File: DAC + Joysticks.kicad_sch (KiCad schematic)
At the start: 127 parts, among them J10 L Phono, J11 R Phono, J8 JOY0, J9 JOY1, U23 74HC374, U24 74HC374, U25 74HC244, U26 74HC244, U27 74HC373, U28 74HC244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

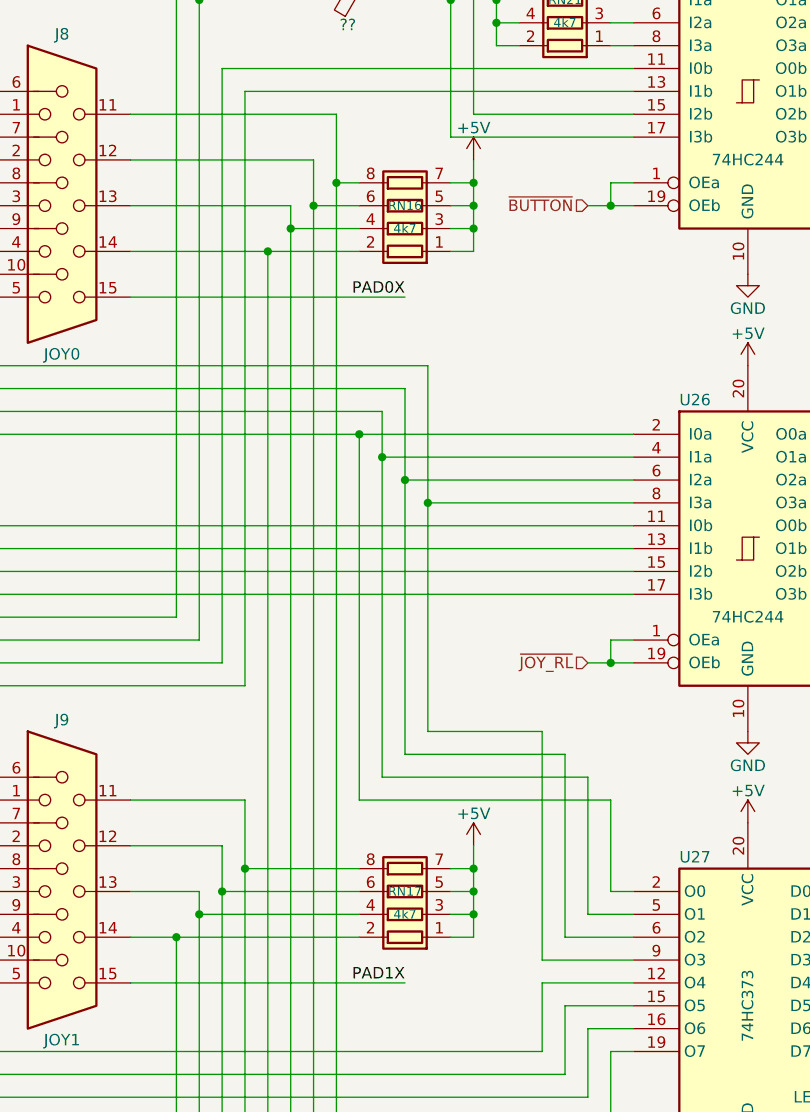
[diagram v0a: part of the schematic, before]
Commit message: motherboard: Routing for the joystick ports
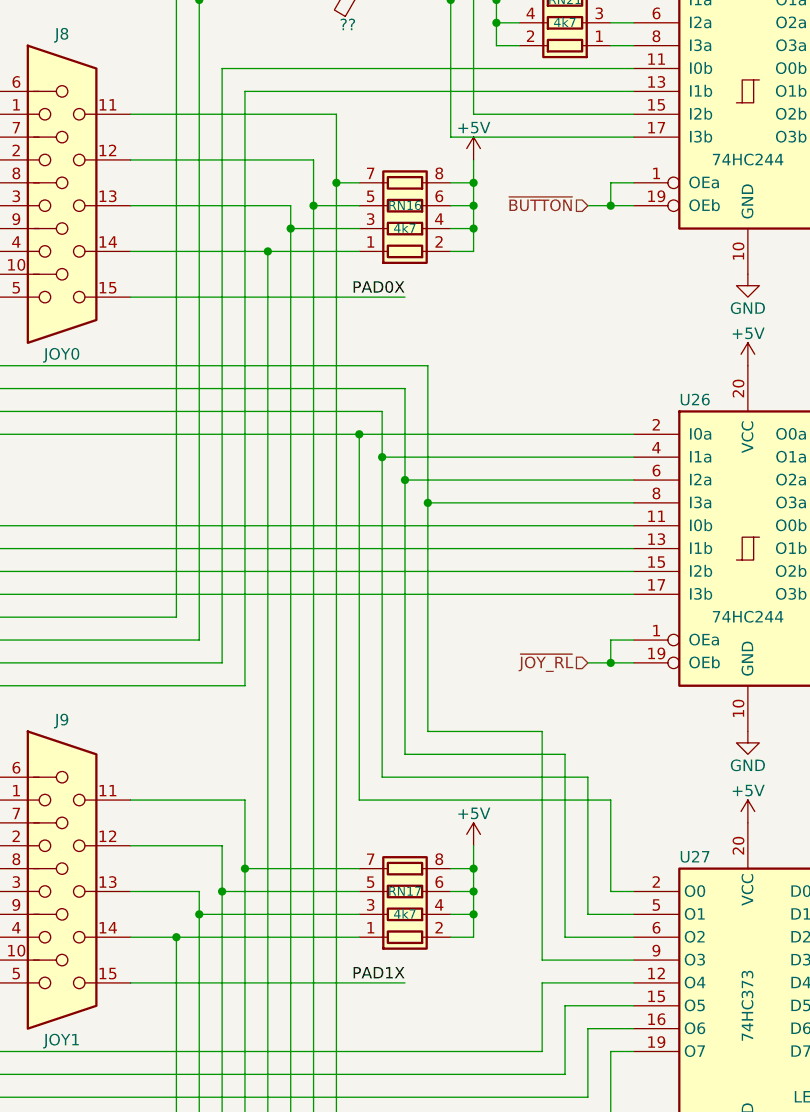
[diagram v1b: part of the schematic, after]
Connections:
- net +5V: now also RN16.2 (R2.1), RN16.4 (R4.1), RN16.6 (R3.2), RN16.8 (R1.2), RN17.2 (R2.1), RN17.4 (R4.1), RN17.6 (R3.2), RN17.8 (R1.2); no longer RN16.1 (R1.1), RN16.3 (R3.1), RN16.5 (R4.2), RN16.7 (R2.2), RN17.1 (R1.1), RN17.3 (R3.1), RN17.5 (R4.2), RN17.7 (R2.2)
- net at J9.14, U28.11 (I0b): now also RN17.1 (R1.1); no longer RN17.2 (R2.1)
- net at J9.13, U28.13 (I1b): now also RN17.3 (R3.1); no longer RN17.4 (R4.1)
- net at J9.12, U28.15 (I2b): now also RN17.5 (R4.2); no longer RN17.6 (R3.2)
- net at J9.11, U28.17 (I3b): now also RN17.7 (R2.2); no longer RN17.8 (R1.2)
- net at J8.14, U28.2 (I0a): now also RN16.1 (R1.1); no longer RN16.2 (R2.1)
- net at J8.13, U28.4 (I1a): now also RN16.3 (R3.1); no longer RN16.4 (R4.1)
- net at J8.12, U28.6 (I2a): now also RN16.5 (R4.2); no longer RN16.6 (R3.2)
- net at J8.11, U28.8 (I3a): now also RN16.7 (R2.2); no longer RN16.8 (R1.2)
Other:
- moved on the sheet: RN16, RN17
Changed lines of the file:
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@@
 	(symbol
 		(lib_id "dragonmux:R_Pack04_OddEven")
-		(at 101.6 63.5 90)
+		(at 101.6 63.5 270)
+		(mirror x)
 		(unit 1)
 		(exclude_from_sim no)
@@
 		)
 		(property "Description" "4 resistor network, parallel topology"
-			(at 114.3 64.77 0)
+			(at 88.9 64.77 0)
 			(effects
 				(font
@@
 	(symbol
 		(lib_id "dragonmux:R_Pack04_OddEven")
-		(at 101.6 139.7 90)
+		(at 101.6 139.7 270)
+		(mirror x)
 		(unit 1)
 		(exclude_from_sim no)
@@
 		)
 		(property "Description" "4 resistor network, parallel topology"
-			(at 114.3 140.97 0)
+			(at 88.9 140.97 0)
 			(effects
 				(font

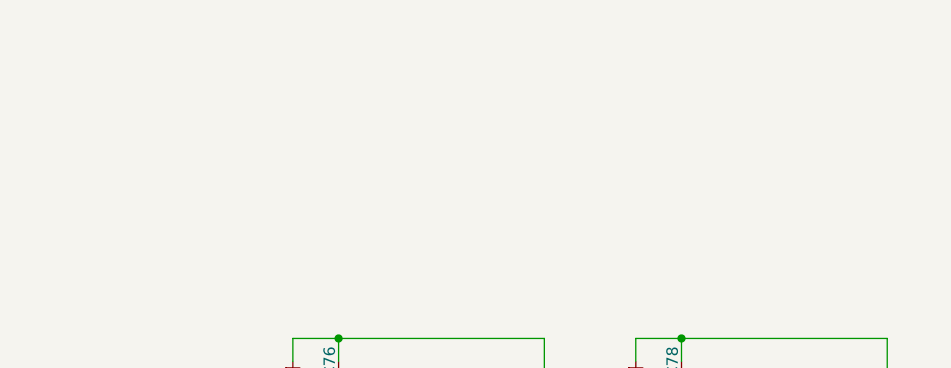
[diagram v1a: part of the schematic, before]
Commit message: motherboard: Added a note about how the FCLK signal works and how the Butterworth filter cutoffs work
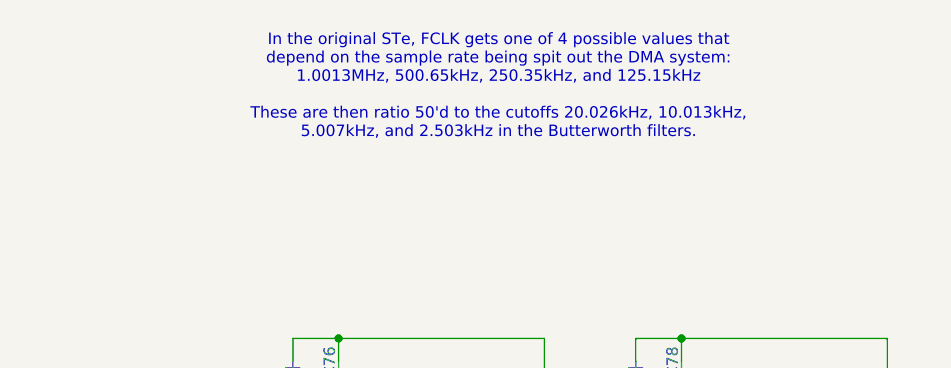
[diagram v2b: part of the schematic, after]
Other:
- note added: "In the original STe, FCLK gets one of 4 possible values that depend on the sample rate being spit out the DMA system: 1.0013MHz, 500.65kHz, 250.35kHz, and 125.15kHz These are then ratio 50'd to the cutoffs 20.026kHz, 10.013kHz, 5.007kHz, and 2.503kHz in the Butterworth filters."
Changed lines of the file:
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@@
 		(members "D[0..7]")
+	)
+	(text "In the original STe, FCLK gets one of 4 possible values that\ndepend on the sample rate being spit out the DMA system:\n1.0013MHz, 500.65kHz, 250.35kHz, and 125.15kHz\n\nThese are then ratio 50'd to the cutoffs 20.026kHz, 10.013kHz,\n5.007kHz, and 2.503kHz in the Butterworth filters."
+		(exclude_from_sim no)
+		(at 355.6 25.4 0)
+		(effects
+			(font
+				(size 1.27 1.27)
+			)
+		)
 	)
 	(junction

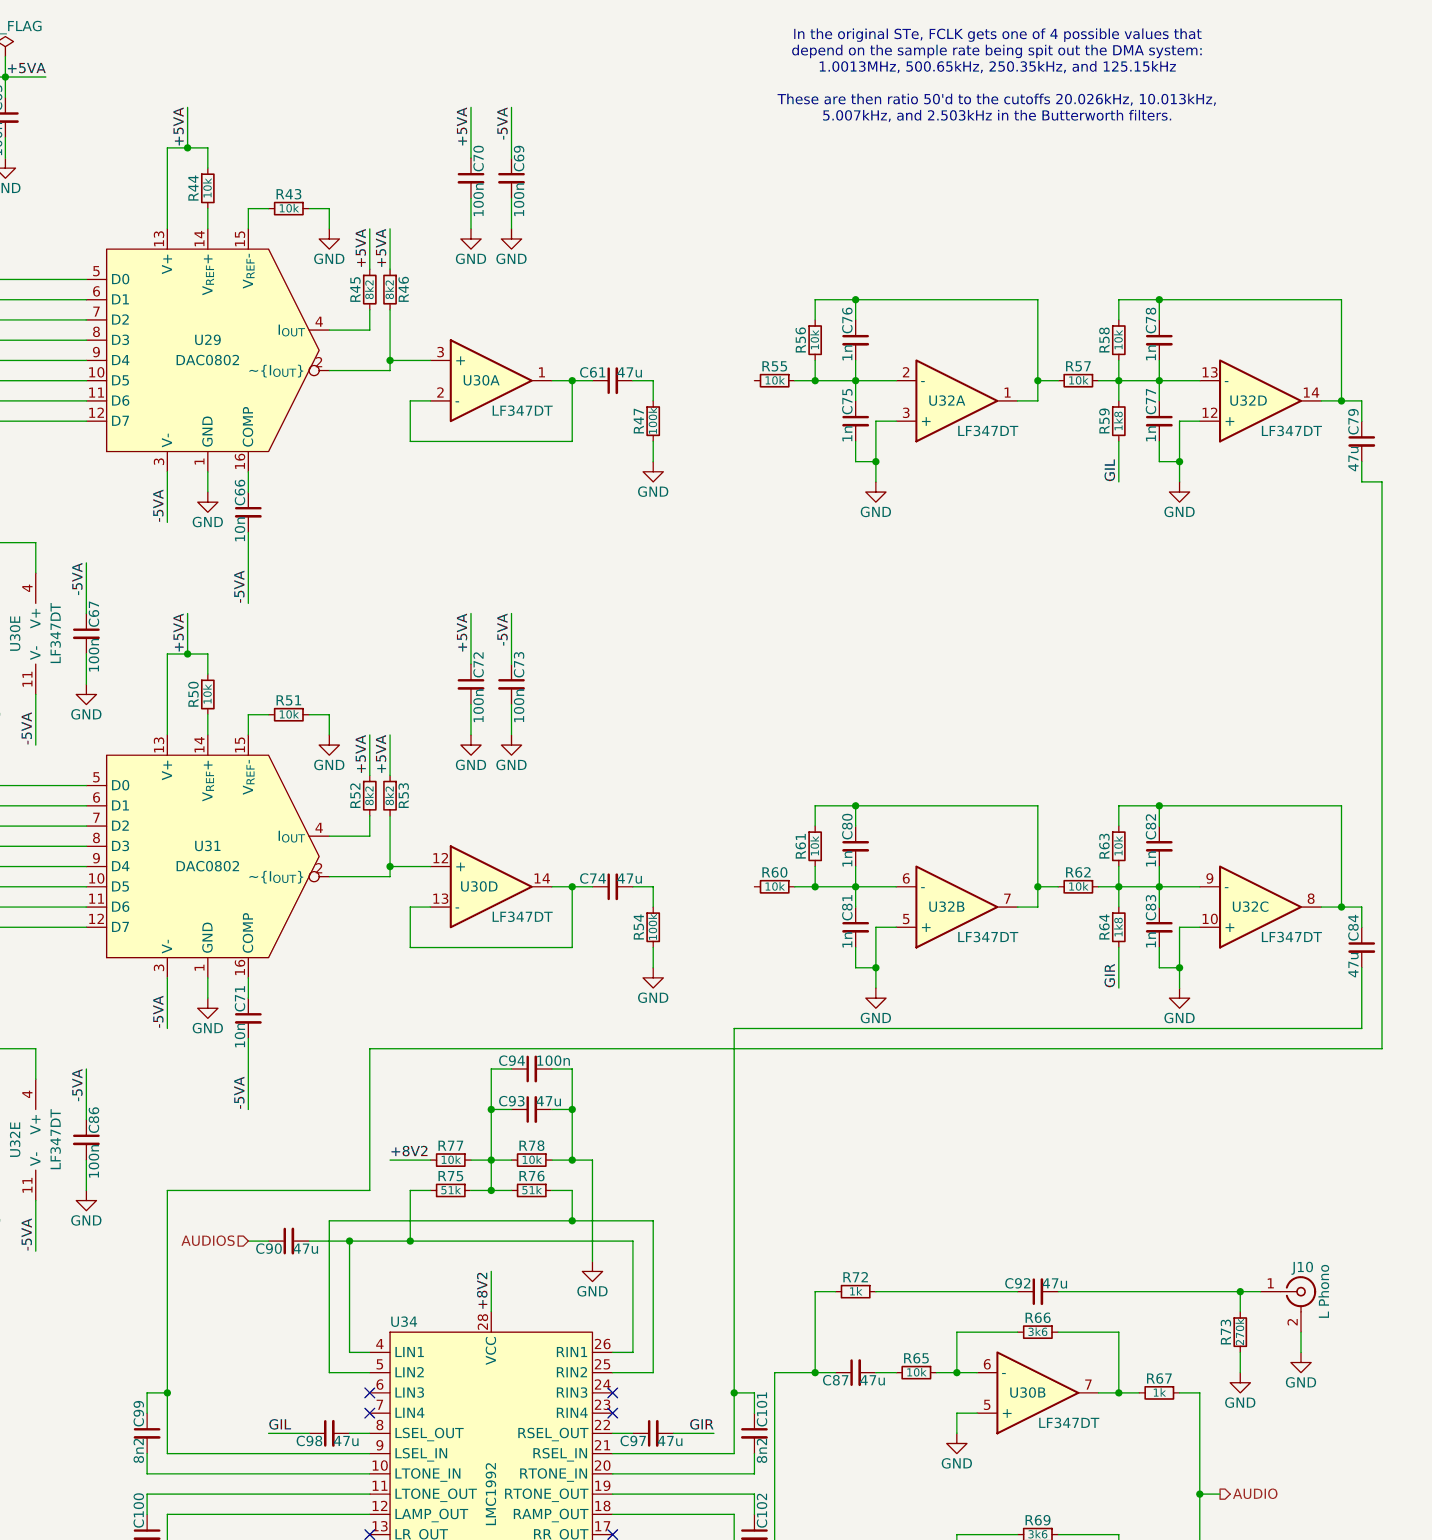
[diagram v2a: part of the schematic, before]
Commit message: motherboard: Added the Butterworth filters for the audio paths so they work correctly
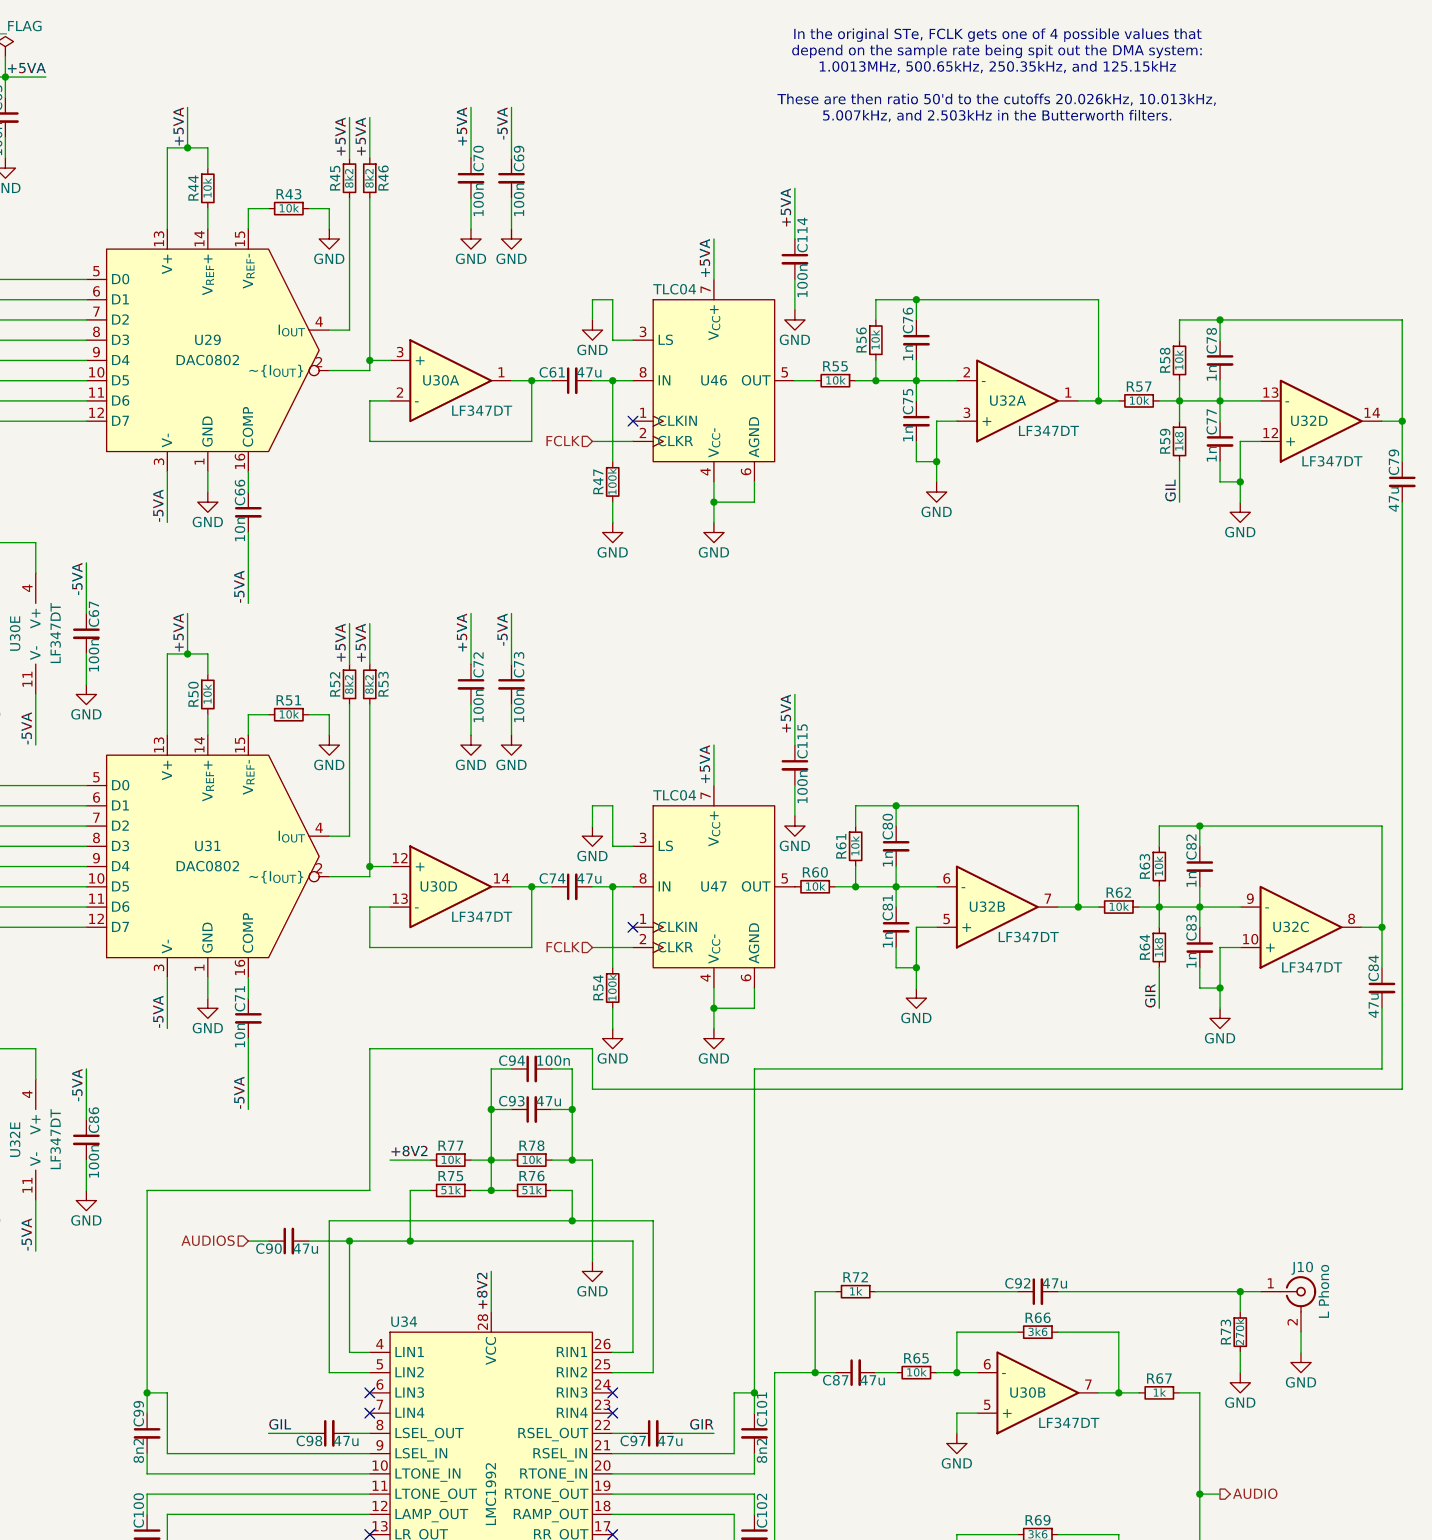
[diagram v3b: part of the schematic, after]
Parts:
- added C114, C115: 100n, rhais_rcl:C0603, symbol Device:C_Small
- added U46, U47: TLC04, rhais_package-smd:SO-8_3.9x4.9mm_P1.27mm, symbol dragonSTe:TLC04
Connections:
- net +5VA: now also C114.1, C115.1, U46.7 (V_{CC}+), U47.7 (V_{CC}+)
- net GND: now also C114.2, C115.2, U46.3 (LS), U46.4 (V_{CC}-), U46.6 (AGND), U47.3 (LS), U47.4 (V_{CC}-), U47.6 (AGND)
- net at C74.2, R54.1: now also U47.8 (IN)
- net at R55.2: now also U46.5 (OUT)
- net at C61.2, R47.1: now also U46.8 (IN)
- net at R60.2: now also U47.5 (OUT)
- new net FCLK: U46.2 (CLKR), U47.2 (CLKR)
- no-connect marks 8 -> 10
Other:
- moved on the sheet: C61, C74, C75, C76, C77, C78, C79, C80, C81, C82, C83, C84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
